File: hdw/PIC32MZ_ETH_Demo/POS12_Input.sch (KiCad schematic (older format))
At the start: 20 parts

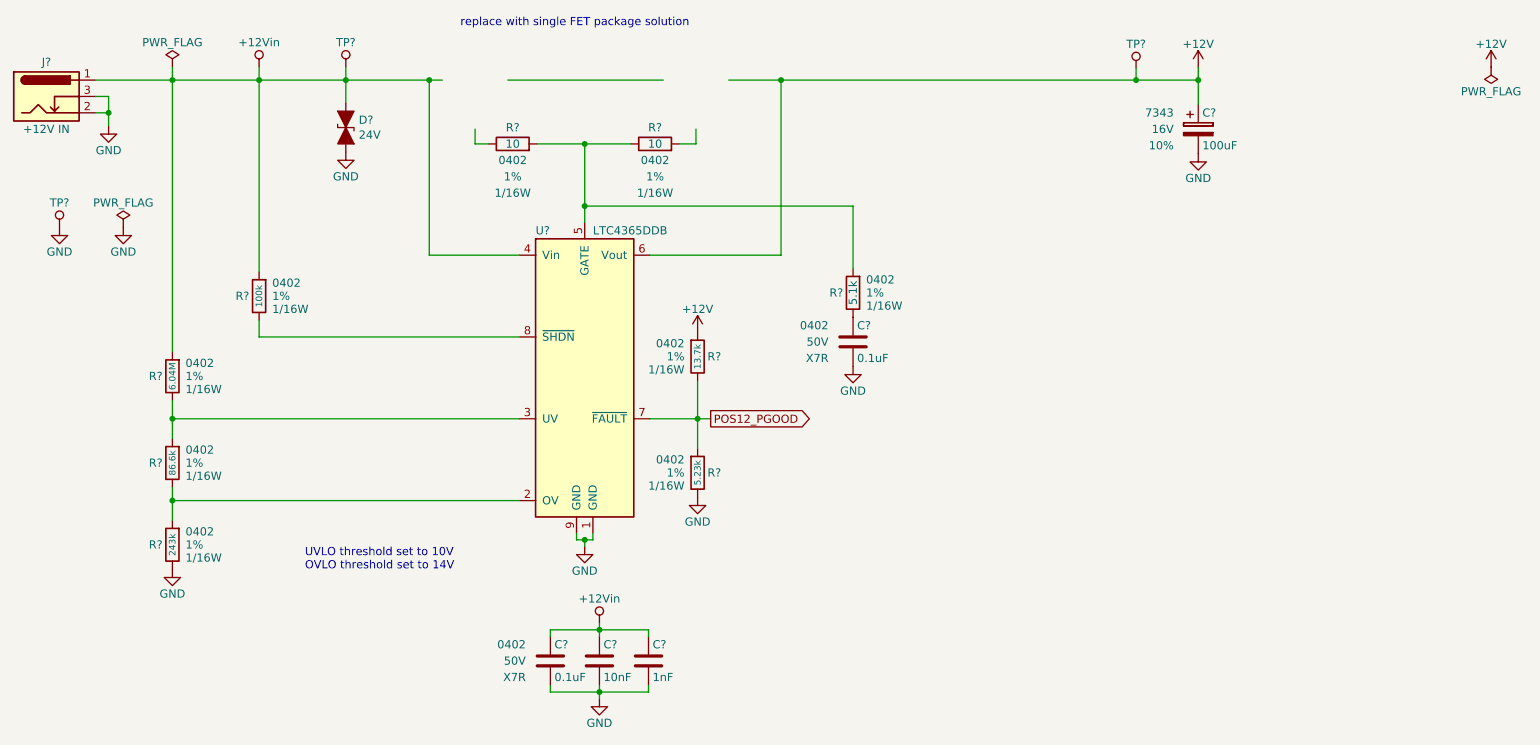
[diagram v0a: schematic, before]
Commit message: More schematic tweaks, followed PHY design guide
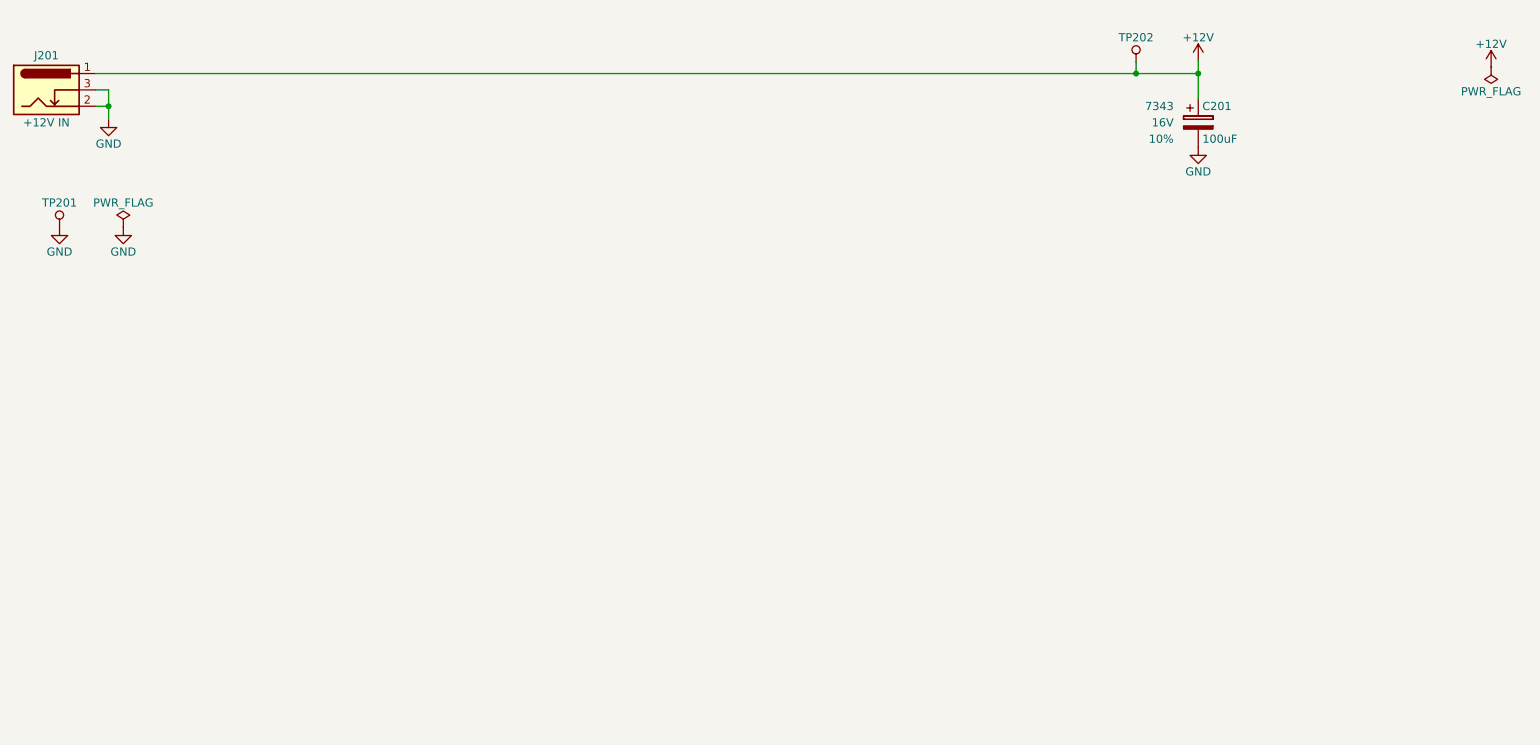
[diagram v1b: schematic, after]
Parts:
- removed C? (x2): 0.1uF, Capacitors_SMD:C_0402, symbol Custom_Library:C_Custom
- removed C?: 10nF, Capacitors_SMD:C_0402, symbol Custom_Library:C_Custom
- removed C?: 1nF, Capacitors_SMD:C_0402, symbol Custom_Library:C_Custom
- removed D?: 24V, Diodes_SMD:D_SMA, symbol Device:D_TVS_ALT
- removed R?: 6.04M, Resistors_SMD:R_0402, symbol Custom_Library:R_Custom
- removed R?: 86.6k, Resistors_SMD:R_0402, symbol Custom_Library:R_Custom
- removed R?: 243k, Resistors_SMD:R_0402, symbol Custom_Library:R_Custom
- removed R?: 100k, Resistors_SMD:R_0402, symbol Custom_Library:R_Custom
- removed R? (x2): 10, Resistors_SMD:R_0402, symbol Custom_Library:R_Custom
- removed R?: 5.1k, Resistors_SMD:R_0402, symbol Custom_Library:R_Custom
- removed R?: 13.7k, Resistors_SMD:R_0402, symbol Custom_Library:R_Custom
- removed R?: 5.23k, Resistors_SMD:R_0402, symbol Custom_Library:R_Custom
- removed TP?: TP, Custom Footprints Library:Test_Point, symbol Custom_Library:TP
- removed U?: LTC4365DDB, Housings_DFN_QFN:DFN-8-1EP_2x3mm_Pitch0.5mm, symbol Custom_Library:LTC4365DDB
- gave numbers to parts that had none: 4
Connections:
- net labels removed: +12Vin, POS12_PGOOD
- wire segments 65 -> 9
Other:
- note removed: "UVLO threshold set to 10V\nOVLO threshold set to 14V"
- note removed: "replace with single FET package solution"
- moved on the sheet: C201, J201, TP202

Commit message: Populated digi-key pn's
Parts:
- J201: Digi-Key PN CP-202BH-ND -> (none)
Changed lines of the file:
@@
 F 2 "Connectors:BARREL_JACK" H 1200 2290 50  0001 C CNN
 F 3 "~" H 1200 2290 50  0001 C CNN
-F 4 "CP-202BH-ND" H -1010 -700 50  0001 C CNN "Digi-Key PN"
+F 4 "" H -1010 -700 50  0001 C CNN "Digi-Key PN"
 	1    1150 2330
 	1    0    0    -1
